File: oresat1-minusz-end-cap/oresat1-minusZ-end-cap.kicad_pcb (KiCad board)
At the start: 4 copper layers, 105.6 x 105.6 mm, 47 parts, among them J1 M55-7011242R, J2 U.FL-R-SMA, U1 RM3100, U2 RM3100

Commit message: routine push
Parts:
- moved C2 7.65 mm to (117.7, 122.7)
- moved L8 7.65 mm to (113.1, 124.6)
- moved L9 7.65 mm to (106.9, 119.2)
- moved R10 7.65 mm to (115.5, 120.5)
- moved R11 7.65 mm to (115.5, 117.5)
- moved R13 7.65 mm to (114.3, 122.7)
- moved R14 7.65 mm to (109.3, 119.7)
- moved R9 7.65 mm to (112.5, 114.6)
- moved C1 7.65 mm to (114.4, 114.6)
- moved U1 7.65 mm to (112.5, 118.4)
- moved L7 7.65 mm to (117.6, 118.4)
- moved R15 7.65 mm to (110.7, 121.6)
- moved R12 7.65 mm to (111.4, 122.8)
- moved C4 0.20 mm to (182.0, 75.0)
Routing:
- net /MAG-SCL: track 135.0 -> 142.4 mm
- net /MAG-SDA: track 116.1 -> 121.7 mm

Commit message: routine push
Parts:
- added R16: 121, oresat-passives:0603-C-NOSILK, F.Cu at (105.1, 114.0)
- added R17: 121, oresat-passives:0603-C-NOSILK, F.Cu at (104.0, 114.0)
- added R18: 121, oresat-passives:0603-C-NOSILK, F.Cu at (108.4, 114.0)
- added R19: 121, oresat-passives:0603-C-NOSILK, F.Cu at (107.3, 114.0)
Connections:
- J1 pad MP: GND -> (no net)
- U1 pad 28: +3.3v -> Net-(U1-MISO/SA1)
- U1 pad 3: GND -> Net-(U1-SSN/SA0)
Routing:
- net Net-(U1-MISO/SA1): track 0.00 -> 8.33 mm, vias 0 -> 2
- net Net-(U1-SSN/SA0): track 0.00 -> 5.56 mm
- net GND: track 17.4 -> 15.8 mm
- net +3.3v: track 25.1 -> 26.2 mm, vias 26 -> 27
- net /MAG-SCL: track 142.4 -> 143.0 mm

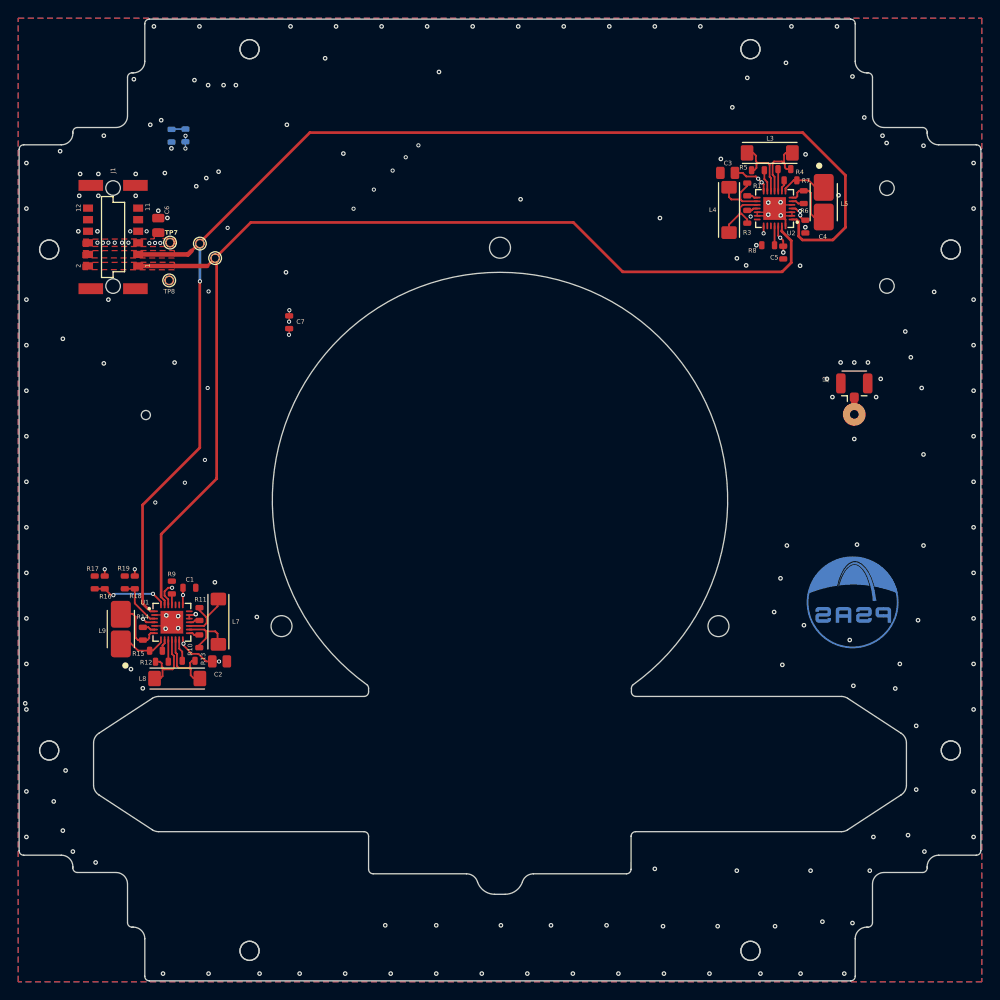
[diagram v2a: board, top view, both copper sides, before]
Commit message: Brought -Z end cap up to the current state. Added address resistors, fixed capacitor placement, polished and made PNI layout consistent, added makefile and readme.
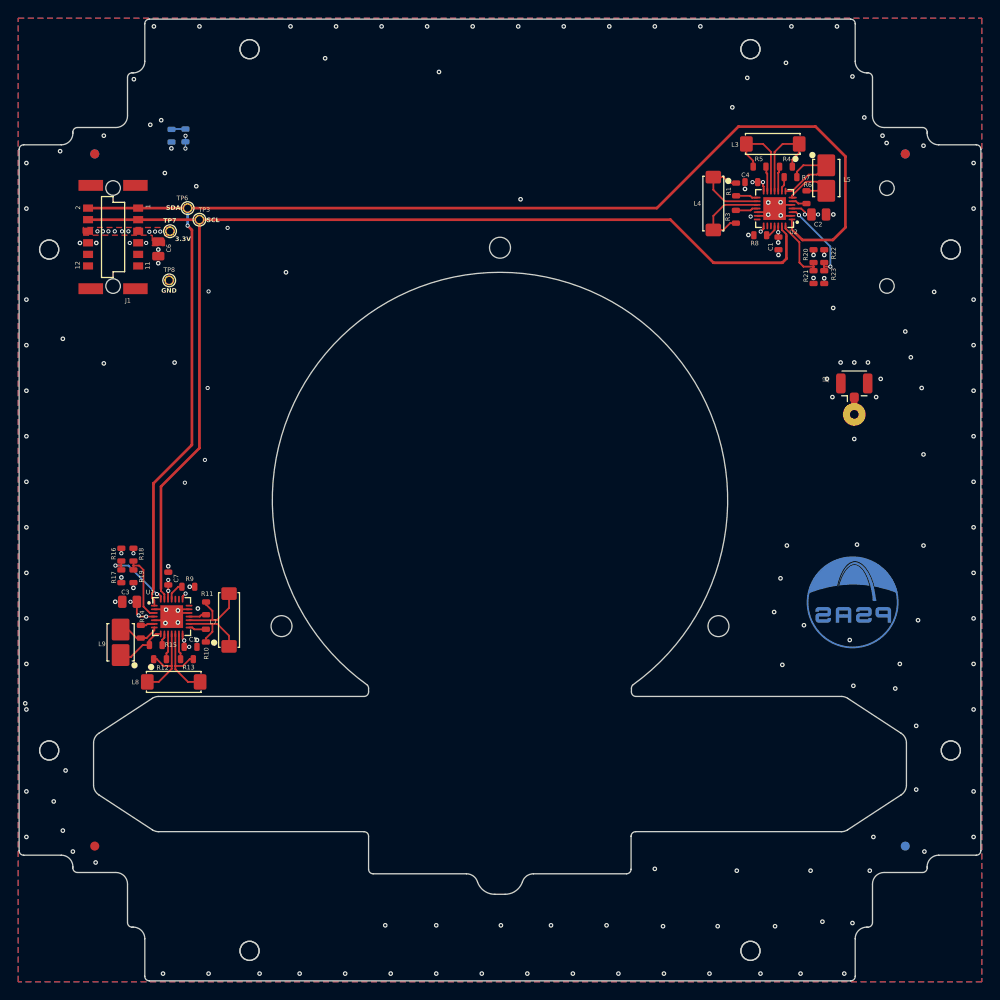
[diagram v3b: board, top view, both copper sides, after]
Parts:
- added FID101: Fiducial, Fiducial:Fiducial_1mm_Mask2mm, F.Cu at (104.0, 67.0)
- added FID102: Fiducial, Fiducial:Fiducial_1mm_Mask2mm, F.Cu at (193.0, 67.0)
- added FID103: Fiducial, Fiducial:Fiducial_1mm_Mask2mm, F.Cu at (104.0, 143.0)
- added FID104: Fiducial, Fiducial:Fiducial_1mm_Mask2mm, B.Cu at (193.0, 67.0)
- added FID105: Fiducial, Fiducial:Fiducial_1mm_Mask2mm, B.Cu at (104.0, 67.0)
- added FID106: Fiducial, Fiducial:Fiducial_1mm_Mask2mm, B.Cu at (193.0, 143.0)
- added R20: 121, oresat-passives:0603-C-NOSILK, F.Cu at (182.9, 78.2)
- added R21: 121, oresat-passives:0603-C-NOSILK, F.Cu at (182.9, 80.5)
- added R22: 121, oresat-passives:0603-C-NOSILK, F.Cu at (184.1, 78.2)
- added R23: 121, oresat-passives:0603-C-NOSILK, F.Cu at (184.1, 80.5)
- J1: footprint oresat-connectors:J-Harwin-M55-60X1242R -> oresat-connectors:J-Harwin-M55-7XX1242R
- U1, U2: footprint oresat-misc:RM3100-MagI2C -> oresat-ics:U-PNI-RM3100-IC
- moved C2 82.1 mm to (183.5, 73.7)
- moved C3 80.8 mm to (107.8, 116.2)
- moved C5 78.2 mm to (114.5, 121.1), turned to 0 degrees
- moved C1 74.9 mm to (179.1, 76.8), turned to -90 degrees
- moved C7 31.1 mm to (112.1, 113.6), turned to 90 degrees
- moved C4 7.67 mm to (176.1, 70.1), turned to 180 degrees
- moved TP6 6.27 mm to (114.2, 73.0)
- moved R16 3.55 mm to (106.9, 111.0)
- moved R18 3.05 mm to (108.2, 111.0)
- moved R17 3.00 mm to (106.9, 113.4), turned to -90 degrees
- moved L5 2.66 mm to (184.3, 69.7)
- moved TP3 2.63 mm to (115.5, 74.2)
- moved C6 2.58 mm to (111.0, 77.4), turned to -90 degrees
- moved L4 1.86 mm to (171.9, 72.5), turned to -90 degrees
- moved R9 1.81 mm to (114.3, 114.5), turned to 180 degrees
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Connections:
- J1 pad MP: (no net) -> GND
- U1 pad 1: /MAG-SCL -> /MAG-SDA
- U1 pad 27: /MAG-SDA -> /MAG-SCL
- U2 pad 1: /MAG-SCL -> /MAG-SDA
- U2 pad 27: /MAG-SDA -> /MAG-SCL
- U2 pad 28: GND -> Net-(U2-MISO/SA1)
- U2 pad 3: GND -> Net-(U2-SSN/SA0)
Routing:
- net /MAG-SDA: track 121.7 -> 149.8 mm, vias 0 -> 1
- net /MAG-SCL: track 143.0 -> 126.2 mm, vias 1 -> 0
- net Net-(U2-SSN/SA0): track 0.00 -> 9.60 mm, vias 0 -> 2
- net Net-(U2-MISO/SA1): track 0.00 -> 7.30 mm
- net +3.3v: track 26.2 -> 20.5 mm, vias 27 -> 30
- net GND: track 15.8 -> 10.8 mm, vias 187 -> 164
- net Net-(U2-ZINN): track 5.19 -> 9.77 mm
- net Net-(U2-XINP): track 6.31 -> 9.50 mm
- net Net-(U2-XINN): track 6.72 -> 9.65 mm
- net Net-(U1-XINN): track 6.67 -> 9.09 mm
- net Net-(U1-SSN/SA0): track 5.56 -> 7.78 mm
- net Net-(U2-YINN): track 7.58 -> 9.59 mm
- net Net-(U1-XINP): track 6.47 -> 8.38 mm
- net Net-(U1-YINN): track 7.59 -> 9.46 mm
- net Net-(U2-YINP): track 7.73 -> 9.58 mm
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- removed copper zone on F.Cu, net /MAG-SCL
- removed copper zone on F.Cu, net /MAG-SDA
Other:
- outline, holes or cut-outs redrawn
- board text added: "3.3V"
- board text added: "GND"
- board text added: "SCL"
- board text added: "SDA"

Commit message: Bring BOM up to date
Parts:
- L3: value SEN2-XY (y-axis) -> RM3100-XY
- L4: value SEN2-XY (x-axis) -> RM3100-XY
- L5: value SEN2-Z (z-axis) -> RM3100-Z
- L7: value SEN1-XY (x-axis) -> RM3100-XY
- L8: value SEN1-XY (y-axis) -> RM3100-XY
- L9: value SEN1-Z (z-axis) -> RM3100-Z

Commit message: Polishing layout, mostly stiching
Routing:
- net GND: vias 164 -> 193
